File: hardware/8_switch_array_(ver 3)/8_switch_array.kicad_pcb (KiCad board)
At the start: 2 copper layers, 45.5 x 48.5 mm, 20 parts, among them J1 Conn_01x04, J10 Conn_01x02, J11 Conn_01x02, J12 Conn_01x02, J2 Conn_01x04, J3 Conn_01x02, J4 Conn_01x02, J5 Conn_01x02, J6 Conn_01x02, J7 Conn_01x02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

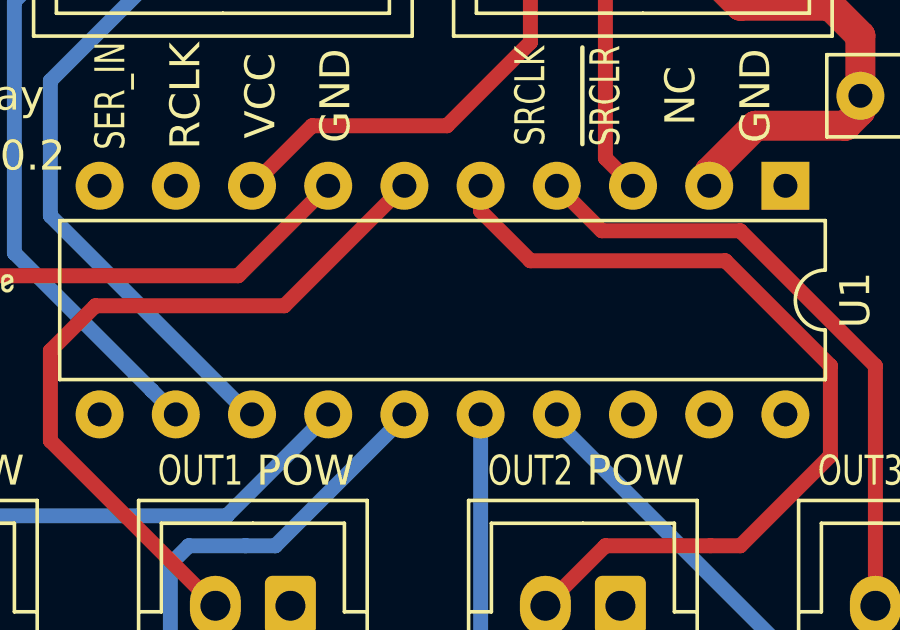
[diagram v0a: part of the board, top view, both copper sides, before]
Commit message: Apply CERN-W license
Apply CERN-W license to all boards, move the first iteration of the IR_sensor to the archive

Co-Authored-By: Andre Maia Chagas <a.maia-chagas@sussex.ac.uk>
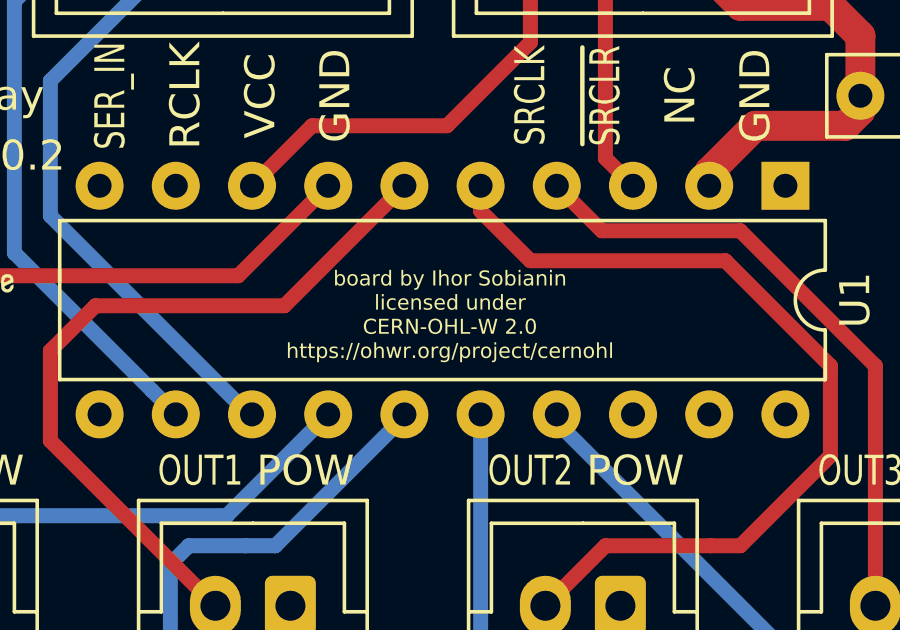
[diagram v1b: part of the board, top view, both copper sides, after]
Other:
- board text added: "board by Ihor Sobianin licensed under CERN-OHL-W 2.0 https://ohwr.org/project/cernohl"
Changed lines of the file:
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@@
   (general
     (thickness 1.6)
-    (drawings 70)
+    (drawings 71)
     (tracks 99)
     (zones 0)
@@
   )
   (setup
-    (last_trace_width 1)
+    (last_trace_width 0.25)
     (user_trace_width 0.5)
     (user_trace_width 1)
@@
     (visible_elements 7FFFFF7F)
     (pcbplotparams
-      (layerselection 0x3ffff_ffffffff)
+      (layerselection 0x00030_7ffffffe)
       (usegerberextensions false)
       (usegerberattributes false)
@@
       (effects (font (size 1 1) (thickness 0.15)))
     )
-    (fp_text user %R (at 3.81 11.43 90) (layer F.Fab)
-      (effects (font (size 1 1) (thickness 0.15)))
-    )
-    (fp_arc (start 3.81 -1.33) (end 2.81 -1.33) (angle -180) (layer F.SilkS) (width 0.12))
     (fp_line (start 1.635 -1.27) (end 6.985 -1.27) (layer F.Fab) (width 0.1))
     (fp_line (start 6.985 -1.27) (end 6.985 24.13) (layer F.Fab) (width 0.1))
@@
     (fp_line (start 8.7 24.4) (end 8.7 -1.55) (layer F.CrtYd) (width 0.05))
     (fp_line (start 8.7 -1.55) (end -1.1 -1.55) (layer F.CrtYd) (width 0.05))
+    (fp_text user %R (at 3.81 11.43 90) (layer F.Fab)
+      (effects (font (size 1 1) (thickness 0.15)))
+    )
+    (fp_arc (start 3.81 -1.33) (end 2.81 -1.33) (angle -180) (layer F.SilkS) (width 0.12))
     (pad 20 thru_hole oval (at 7.62 0 270) (size 1.6 1.6) (drill 0.8) (layers *.Cu *.Mask)
       (net 1 GND))
@@
     )
   )
+  (gr_text "board by Ihor Sobianin\nlicensed under\nCERN-OHL-W 2.0\nhttps://ohwr.org/project/cernohl" (at 147.32 50.8) (layer F.SilkS)
+    (effects (font (size 0.5 0.5) (thickness 0.1)))
+  )
   (gr_text v0.2 (at 133 45.5) (layer F.SilkS)
